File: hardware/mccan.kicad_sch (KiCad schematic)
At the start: 0 parts

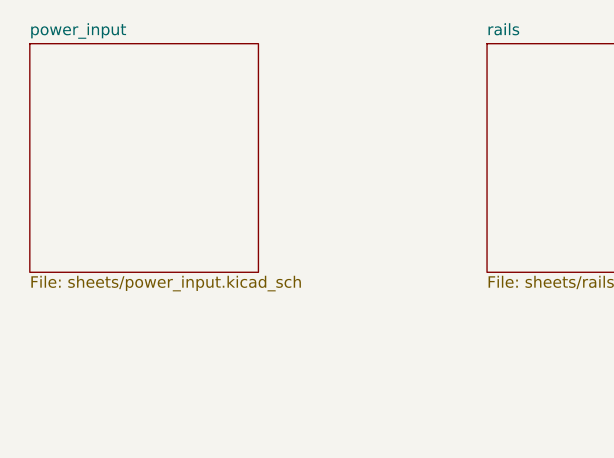
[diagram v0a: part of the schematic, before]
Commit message: chore(hw): adopt KiCad's canonical files after first GUI open
You opened the project in KiCad and it rewrote the hand-authored files into its
own canonical form. Verified equivalent before committing: the power_input
netlist is UNCHANGED net-for-net -- all nine nets identical, and GND_IN and GND
are still genuinely separate with an empty intersection. Nothing was lost in a
3106-line reformat.

CORRECTION TO MY EARLIER CHANGE (d829e26). I added per-sheet (instances) blocks
to the root schematic and concluded they were canonical because
"kicad-cli sch upgrade" round-tripped them byte-identically. The GUI disagrees:
on open, KiCad stripped all four blocks and kept only the root's own
(sheet_instances (path "/" (page "1"))).

So the premise was wrong in both directions. There was no malformed hierarchy to
repair -- KiCad simply does not store per-sheet page numbers in this arrangement
and regenerates what it needs on load. I tested the CLI path and inferred the
GUI's behaviour from it, which was not a safe inference, and the CLI test looked
like confirmation because upgrade genuinely does not touch those blocks.

Net effect: d829e26 was harmless but unnecessary, and this commit is KiCad's own
answer, which beats my reconstruction of it.

Also adopted: mccan.kicad_pro gains ~428 lines of default project settings that
the hand-authored file never had.

Co-Authored-By: Claude Opus 5 <noreply@anthropic.com>
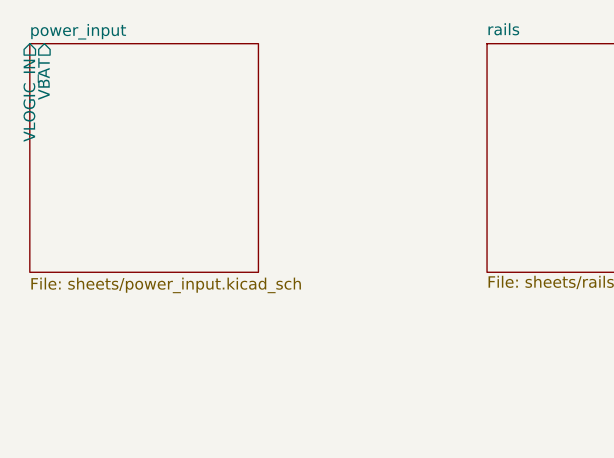
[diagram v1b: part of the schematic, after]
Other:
- sheet power_input ports: added VBAT, VLOGIC_IN; removed none
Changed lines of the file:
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@@
-			)
-		)
-		(instances
-			(project "mccan"
-				(path "/"
-					(page "5")
-				)
 			)
 		)
@@
 			)
 		)
-		(instances
-			(project "mccan"
-				(path "/"
-					(page "3")
-				)
-			)
-		)
 	)
 	(sheet
@@
 			)
 		)
-		(instances
-			(project "mccan"
-				(path "/"
-					(page "4")
-				)
-			)
-		)
 	)
 	(sheet
@@
 		)
 		(property "Sheetname" "power_input"
-			(at 50.8 50.0032 0)
+			(at 50.8 50.0884 0)
 			(show_name no)
 			(do_not_autoplace no)
@@
 		)
 		(property "Sheetfile" "sheets/power_input.kicad_sch"
-			(at 50.8 76.581 0)
+			(at 50.8 76.7846 0)
 			(show_name no)
 			(do_not_autoplace no)
@@
 			)
 		)
-		(instances
-			(project "mccan"
-				(path "/"
-					(page "2")
+		(pin "VLOGIC_IN" output
+			(at 50.8 50.8 90)
+			(effects
+				(font
+					(size 1.27 1.27)
 				)
+				(justify right)
 			)
 		)
+		(pin "VBAT" output
+			(at 52.4193 50.8 90)
+			(effects
+				(font
+					(size 1.27 1.27)
+				)
+				(justify right)
+			)
+		)

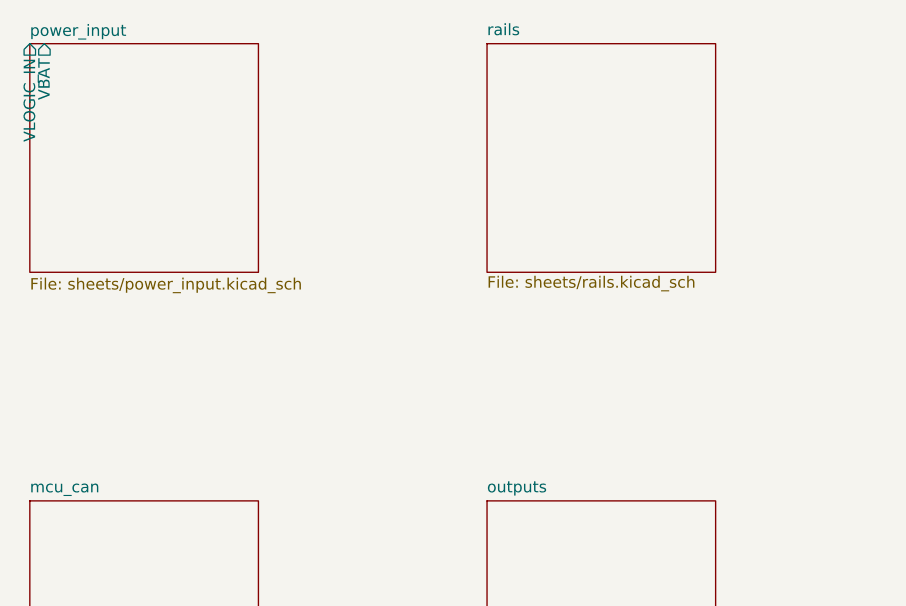
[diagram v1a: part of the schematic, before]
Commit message: hw(rails): finish the rails sheet and fix four defects found on review
The drafting agent's topology was sound but it stopped before finishing, and
verification against the primary datasheets turned up four real problems.

Constant-on-time loop had no ripple to work with.  The LM5164 needs >= 20 mV of
ripple AT FB (datasheet 6.2); an all-ceramic output stage with a feedforward cap
delivered ~3 mV, a 6.5x shortfall.  Replaced with the datasheet's Type-3
injection network on both rails, sized from equations 24-26 and checked against
the >= 12 mV at minimum VIN criterion.  Chosen over adding series ESR because
the ADC sense chain runs off these rails.

Both enables were missing their mandatory pulldowns.  EN_3V3SW and EN_BOOST
reached their pins with nothing else on the net, against the plan's
passive-default table and the LM51571's own "must not be left floating".
Added R19/R20.

The switched 3.3 V rail did not exist.  The load-switch block was dropped when
the sheet was restructured around the boost; added as block 4 with the
DML3017LDC, its mandatory external BLEED resistor and CSR cap.

Symbol pin types were generating false ERC violations -- SW was typed power_in,
so ERC demanded an external driver for the converter's own switch node.

Also corrects two claims in part-selection.md that were written from the feature
list rather than the pin table: the BLEED resistor is external and mandatory,
not an on-chip 100 ohm, and PG is tied to GND rather than pulled up, because a
100k pullup would burn 33 uA of a 100 uA sleep budget.

ERC 26 violations -> 6, all six being root sheet pins whose counterparts live on
mcu_can and outputs, which are not drawn yet.  Netlist verified independently:
VBAT and VLOGIC_IN now span both sheets, EN_3V3SW gates both switched rails, and
the Type-3 nodes are correct on both bucks.

Co-Authored-By: Claude Opus 5 <noreply@anthropic.com>
Claude-Session: https://claude.ai/code/session_01Bkq7QP4he4cdfxkUNzx7DL
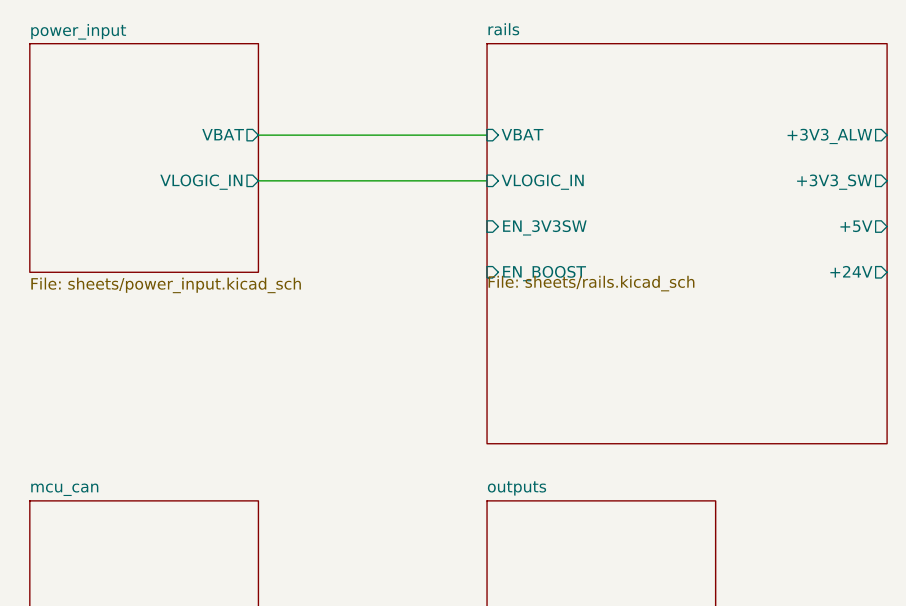
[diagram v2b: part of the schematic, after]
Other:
- sheet rails ports: added +24V, +3V3_ALW, +3V3_SW, +5V, EN_3V3SW, EN_BOOST, VBAT, VLOGIC_IN; removed none
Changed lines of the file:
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@@
 		(comment 1 "Net naming contract: see hardware/README.md")
+	)
+	(wire
+		(pts
+			(xy 76.2 60.96) (xy 101.6 60.96)
+		)
+		(stroke
+			(width 0)
+			(type default)
+		)
+	)
+	(wire
+		(pts
+			(xy 76.2 66.04) (xy 101.6 66.04)
+		)
+		(stroke
+			(width 0)
+			(type default)
+		)
 	)
 	(sheet
@@
 	(sheet
 		(at 101.6 50.8)
-		(size 25.4 25.4)
+		(size 44.45 44.45)
 		(exclude_from_sim no)
 		(in_bom yes)
@@
 			)
 		)
+		(pin "VBAT" input
+			(at 101.6 60.96 180)
+			(effects
+				(font
+					(size 1.27 1.27)
+				)
+				(justify left)
+			)
+		)
+		(pin "VLOGIC_IN" input
+			(at 101.6 66.04 180)
+			(effects
+				(font
+					(size 1.27 1.27)
+				)
+				(justify left)
+			)
+		)
+		(pin "EN_3V3SW" input
+			(at 101.6 71.12 180)
+			(effects
+				(font
+					(size 1.27 1.27)
+				)
+				(justify left)
+			)
+		)
+		(pin "EN_BOOST" input
+			(at 101.6 76.2 180)
+			(effects
+				(font
+					(size 1.27 1.27)
+				)
+				(justify left)
+			)
+		)
+		(pin "+3V3_ALW" output
+			(at 146.05 60.96 0)
+			(effects
+				(font
+					(size 1.27 1.27)
+				)
+				(justify left)
+			)
+		)
+		(pin "+3V3_SW" output
+			(at 146.05 66.04 0)
+			(effects
+				(font
+					(size 1.27 1.27)
+				)
+				(justify left)
+			)
+		)
+		(pin "+5V" output
+			(at 146.05 71.12 0)
+			(effects
+				(font
+					(size 1.27 1.27)
+				)
+				(justify left)
+			)
+		)
+		(pin "+24V" output
+			(at 146.05 76.2 0)
+			(effects
+				(font
+					(size 1.27 1.27)
+				)
+				(justify left)
+			)
+		)
 	)
 	(sheet
@@
 		)
 		(pin "VLOGIC_IN" output
-			(at 50.8 50.8 90)
-			(effects
-				(font
-					(size 1.27 1.27)
-				)
-				(justify right)
+			(at 76.2 66.04 0)
+			(effects
+				(font
+					(size 1.27 1.27)
+				)
+				(justify left)
 			)
 		)
 		(pin "VBAT" output
-			(at 52.4193 50.8 90)
-			(effects
-				(font
-					(size 1.27 1.27)
-				)
-				(justify right)
-			)
-		)
+			(at 76.2 60.96 0)
+			(effects
+				(font
+					(size 1.27 1.27)
+				)
+				(justify left)
+			)
+		)

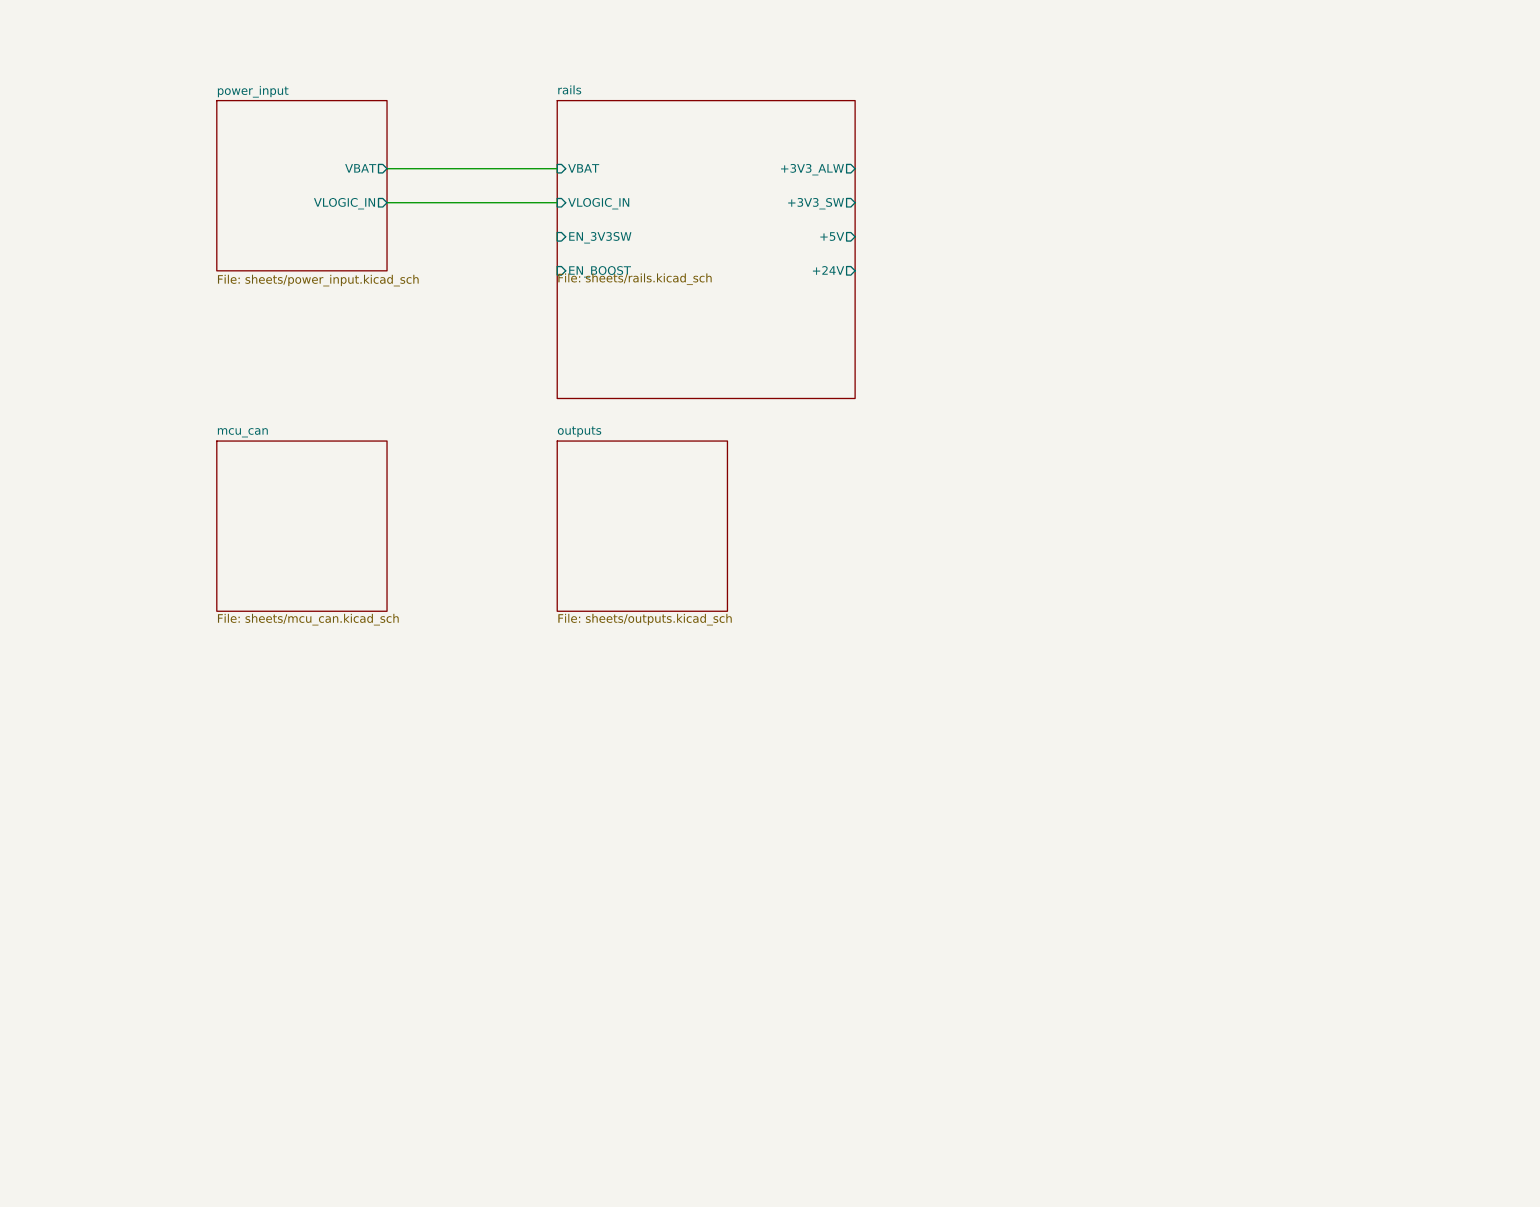
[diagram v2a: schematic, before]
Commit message: hw(sch): ESP32-WROOM-32E-N8, TJA1042 listen-only, prog header (Task 5)
The mcu_can sheet, with every net verified from the exported netlist rather than
from the drawing.  All 24 GPIO assignments match the plan's Global Constraints
table pin for pin.

Listen-only is structural, not a setting.  The netlist shows GPIO 17 reaching
only R23, and the transceiver TXD reaching only R23 and its pull-up, so the DNP
0 ohm link is the single conductive path and a board built to the BOM cannot
assert a dominant bit on the vehicle bus.

The transceiver's two supplies are deliberately split: VIO on +3V3_ALW keeps the
receiver alive so bus traffic still pulls RXD low for EXT0 wake, while VCC on the
switched +5V powers down the transmit side in sleep.  Both pull-ups (TXD, STB)
rest high, so neither costs anything against the sleep budget.

The root schematic is now generated rather than patched, from a declaration of
boxes and pins, with the four sheet UUIDs pinned -- changing one would orphan
every reference designator on that sheet.  Sheet pins join through root-level
labels on stubs; with ~40 inter-sheet nets, wires drawn between the boxes are an
unreadable rat's nest.

Two mechanical defect classes found and now asserted against in the generators:
coordinates must be exact multiples of 1.27 mm (a pin that misses its wire by
0.6 mm looks connected and is not -- 161 instances), and a local label must sit
at a wire's end rather than mid-wire, which forms the net but leaves the endpoint
dangling (14 instances).

Three additions beyond the plan, all flagged in part-selection.md rather than
smuggled in: a pulldown on GPIO 12 (it selects flash voltage at boot and the plan
would have left the strap floating), the new net name IGN_IN for the
ignition-switched sense wire, and putting the MUX/DSEL/DIAG pulldowns on this
sheet because MUX_S3 is GPIO 5, a strapping pin sampled at reset.

ERC: 25 violations, every one of them the outputs sheet not existing yet.

Co-Authored-By: Claude Opus 5 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
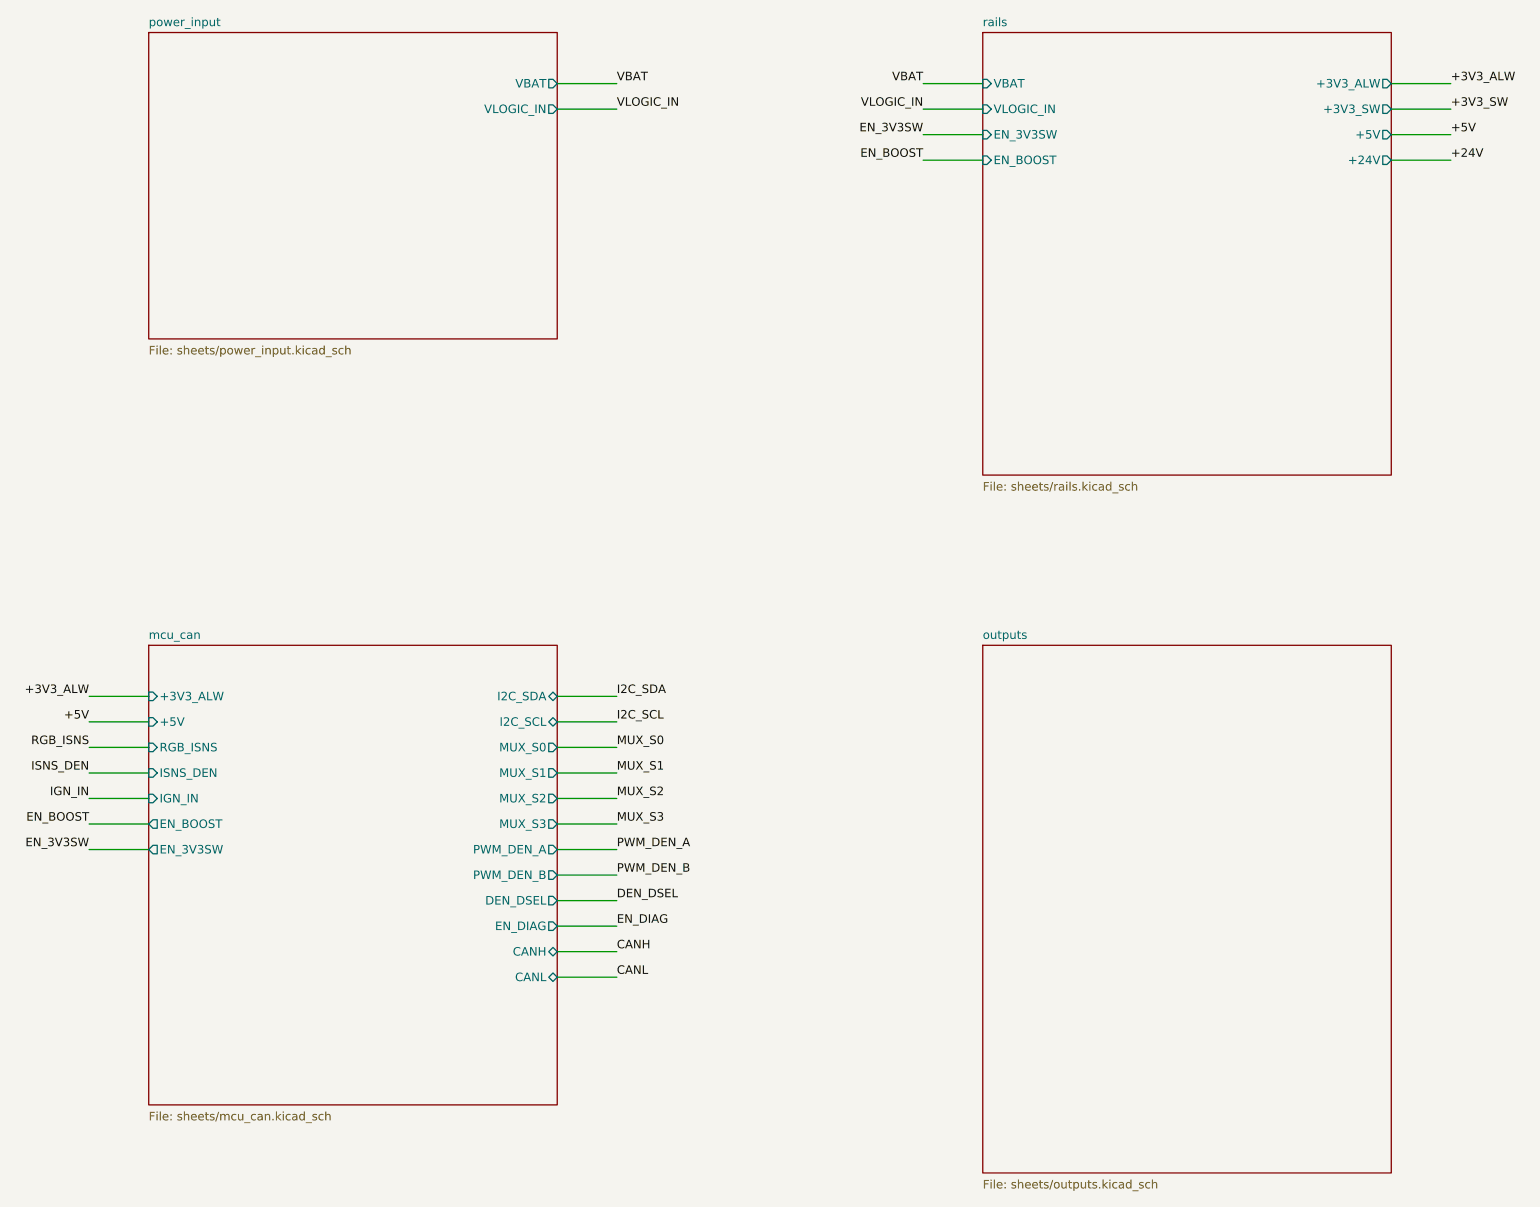
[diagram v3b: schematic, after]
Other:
- sheet mcu_can ports: added +3V3_ALW, +5V, CANH, CANL, DEN_DSEL, EN_3V3SW, EN_BOOST, EN_DIAG, I2C_SCL, I2C_SDA, IGN_IN, ISNS_DEN, MUX_S0, MUX_S1, MUX_S2, MUX_S3, PWM_DEN_A, PWM_DEN_B, RGB_ISNS; removed none
